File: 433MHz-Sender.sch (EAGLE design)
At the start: 21 parts, among them IC1 LP2950Z, U1 ATTINY85V-10S

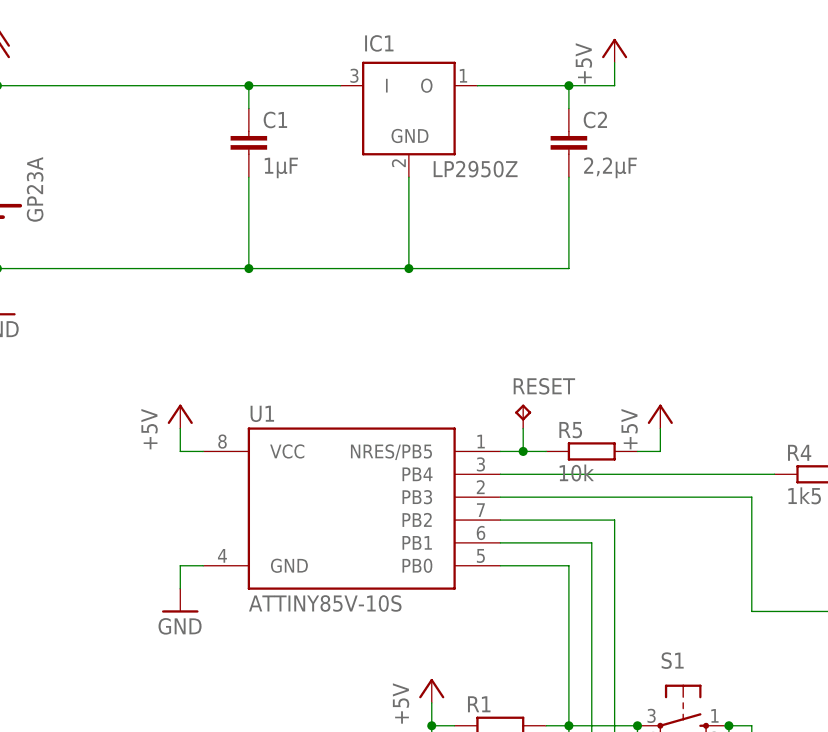
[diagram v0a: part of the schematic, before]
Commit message: 433MHz-Server und IO-Board-2 Anpassungen
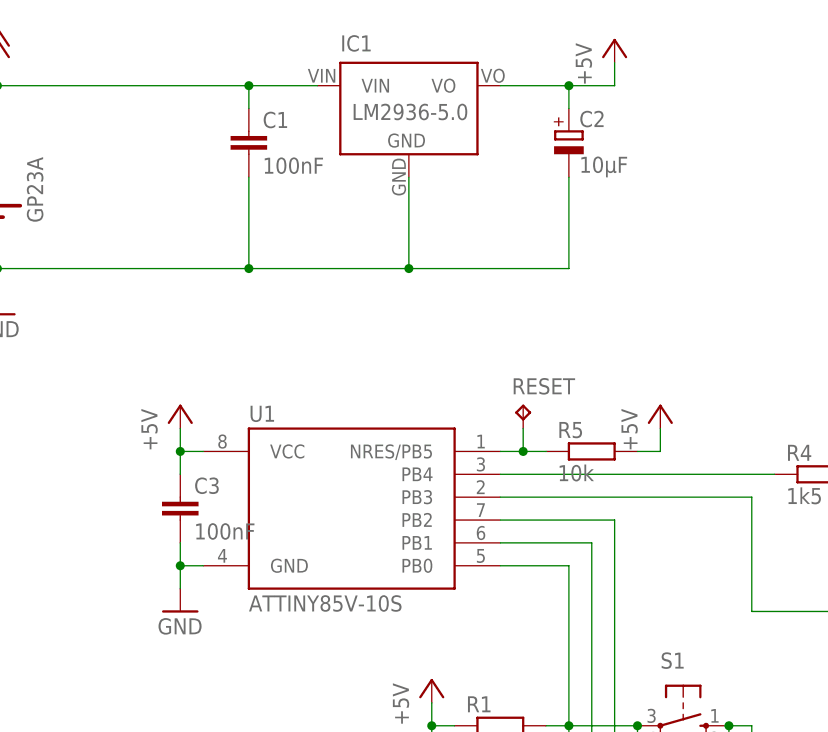
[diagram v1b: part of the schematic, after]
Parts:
- added C3: 100nF, rcl:C-EU025-025X050
- C1: value 1µF -> 100nF
- C2: value 2,2µF -> 10µF; device rcl:C-EU025-025X050 -> rcl:CPOL-EUE2-4
- IC1: value LP2950Z -> LM2936-5.0; device linear:LP2950Z -> LM2936:LM2936-5.0
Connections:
- net +12V: now also IC1.VIN; no longer IC1.I
- net +5V: now also C2.+, C3.1, IC1.VO; no longer C2.1, IC1.O
- net GND: now also C2.-, C3.2; no longer C2.2
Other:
- moved on the sheet: IC1
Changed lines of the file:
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@@
 <setting verticaltext="up"/>
 </settings>
-<grid distance="0.1" unitdist="inch" unit="inch" style="dots" multiple="1" display="yes" altdistance="0.01" altunitdist="inch" altunit="inch"/>
+<grid distance="0.1" unitdist="inch" unit="inch" style="lines" multiple="1" display="no" altdistance="0.01" altunitdist="inch" altunit="inch"/>
 <layers>
 <layer number="1" name="Top" color="4" fill="1" visible="no" active="no"/>
@@
 <part name="P+1" library="supply1" deviceset="+12V" device=""/>
 <part name="GND1" library="supply1" deviceset="GND" device=""/>
-<part name="IC1" library="linear" deviceset="LP2950" device="Z"/>
-<part name="C1" library="rcl" deviceset="C-EU" device="025-025X050" value="1µF"/>
-<part name="C2" library="rcl" deviceset="C-EU" device="025-025X050" value="2,2µF"/>
+<part name="C1" library="rcl" deviceset="C-EU" device="025-025X050" value="100nF"/>
 <part name="P+2" library="supply1" deviceset="+5V" device=""/>
 <part name="P+3" library="supply1" deviceset="+5V" device=""/>
@@
 <part name="R5" library="rcl" deviceset="R-EU_" device="0204/5" value="10k"/>
 <part name="P+6" library="supply1" deviceset="+5V" device=""/>
+<part name="C3" library="rcl" deviceset="C-EU" device="025-025X050" value="100nF"/>
+<part name="IC1" library="LM2936" deviceset="LM2936?*" device="" technology="-5.0"/>
+<part name="C2" library="rcl" deviceset="CPOL-EU" device="E2-4" value="10µF"/>
 </parts>
 <sheets>
@@
 <instance part="P+1" gate="1" x="22.86" y="116.84"/>
 <instance part="GND1" gate="1" x="22.86" y="86.36"/>
-<instance part="IC1" gate="G$1" x="68.58" y="109.22"/>
 <instance part="C1" gate="G$1" x="50.8" y="106.68"/>
-<instance part="C2" gate="G$1" x="86.36" y="106.68"/>
 <instance part="P+2" gate="1" x="91.44" y="116.84"/>
 <instance part="P+3" gate="1" x="43.18" y="76.2"/>
@@
 <instance part="R5" gate="G$1" x="88.9" y="71.12"/>
 <instance part="P+6" gate="1" x="96.52" y="76.2"/>
+<instance part="C3" gate="G$1" x="43.18" y="66.04"/>
+<instance part="IC1" gate="G$1" x="68.58" y="109.22"/>
+<instance part="C2" gate="G$1" x="86.36" y="106.68"/>
 </instances>
 <busses>
@@
 <wire x1="50.8" y1="91.44" x2="22.86" y2="91.44" width="0.1524" layer="91"/>
 <junction x="22.86" y="91.44"/>
+<junction x="50.8" y="91.44"/>
+<wire x1="50.8" y1="91.44" x2="68.58" y2="91.44" width="0.1524" layer="91"/>
+<pinref part="C2" gate="G$1" pin="-"/>
+<wire x1="68.58" y1="91.44" x2="86.36" y2="91.44" width="0.1524" layer="91"/>
+<wire x1="86.36" y1="101.6" x2="86.36" y2="91.44" width="0.1524" layer="91"/>
 <pinref part="IC1" gate="G$1" pin="GND"/>
-<wire x1="50.8" y1="91.44" x2="68.58" y2="91.44" width="0.1524" layer="91"/>
-<wire x1="68.58" y1="91.44" x2="68.58" y2="101.6" width="0.1524" layer="91"/>
-<junction x="50.8" y="91.44"/>
-<pinref part="C2" gate="G$1" pin="2"/>
-<wire x1="68.58" y1="91.44" x2="86.36" y2="91.44" width="0.1524" layer="91"/>
-<wire x1="86.36" y1="91.44" x2="86.36" y2="101.6" width="0.1524" layer="91"/>
+<wire x1="68.58" y1="101.6" x2="68.58" y2="91.44" width="0.1524" layer="91"/>
 <junction x="68.58" y="91.44"/>
 </segment>
@@
 <wire x1="45.72" y1="58.42" x2="43.18" y2="58.42" width="0.1524" layer="91"/>
 <wire x1="43.18" y1="58.42" x2="43.18" y2="55.88" width="0.1524" layer="91"/>
+<pinref part="C3" gate="G$1" pin="2"/>
+<wire x1="43.18" y1="60.96" x2="43.18" y2="58.42" width="0.1524" layer="91"/>
+<junction x="43.18" y="58.42"/>
 </segment>
 <segment>
@@
 <wire x1="22.86" y1="111.76" x2="22.86" y2="114.3" width="0.1524" layer="91"/>
 <wire x1="50.8" y1="111.76" x2="50.8" y2="109.22" width="0.1524" layer="91"/>
-<pinref part="IC1" gate="G$1" pin="I"/>
-<wire x1="50.8" y1="111.76" x2="60.96" y2="111.76" width="0.1524" layer="91"/>
 <wire x1="50.8" y1="111.76" x2="22.86" y2="111.76" width="0.1524" layer="91"/>
+<junction x="22.86" y="111.76"/>
+<pinref part="IC1" gate="G$1" pin="VIN"/>
+<wire x1="50.8" y1="111.76" x2="58.42" y2="111.76" width="0.1524" layer="91"/>
 <junction x="50.8" y="111.76"/>
-<junction x="22.86" y="111.76"/>
 </segment>
 <segment>
@@
 <net name="+5V" class="0">
 <segment>
-<pinref part="IC1" gate="G$1" pin="O"/>
-<wire x1="76.2" y1="111.76" x2="86.36" y2="111.76" width="0.1524" layer="91"/>
-<pinref part="C2" gate="G$1" pin="1"/>
-<wire x1="86.36" y1="111.76" x2="86.36" y2="109.22" width="0.1524" layer="91"/>
-<wire x1="86.36" y1="111.76" x2="91.44" y2="111.76" width="0.1524" layer="91"/>
-<junction x="86.36" y="111.76"/>
 <wire x1="91.44" y1="111.76" x2="91.44" y2="114.3" width="0.1524" layer="91"/>
 <pinref part="P+2" gate="1" pin="+5V"/>
+<pinref part="IC1" gate="G$1" pin="VO"/>
+<wire x1="78.74" y1="111.76" x2="86.36" y2="111.76" width="0.1524" layer="91"/>
+<pinref part="C2" gate="G$1" pin="+"/>
+<wire x1="86.36" y1="111.76" x2="91.44" y2="111.76" width="0.1524" layer="91"/>
+<wire x1="86.36" y1="109.22" x2="86.36" y2="111.76" width="0.1524" layer="91"/>
+<junction x="86.36" y="111.76"/>
 </segment>
 <segment>
@@
 <pinref part="U1" gate="G$1" pin="VCC"/>
 <wire x1="43.18" y1="71.12" x2="45.72" y2="71.12" width="0.1524" layer="91"/>
-</segment>
-<segment>
+<pinref part="C3" gate="G$1" pin="1"/>
+<wire x1="43.18" y1="68.58" x2="43.18" y2="71.12" width="0.1524" layer="91"/>
+<junction x="43.18" y="71.12"/>
+</segment>
+<segment>

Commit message: IO-Board-2 Anpassung
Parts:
- R1, R2, R3: value 10k -> 100k
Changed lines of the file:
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@@
 <part name="433_GND" library="testpad" deviceset="TP" device="PAD1-13"/>
 <part name="GND3" library="supply1" deviceset="GND" device=""/>
-<part name="R1" library="rcl" deviceset="R-EU_" device="0204/5" value="10k"/>
-<part name="R2" library="rcl" deviceset="R-EU_" device="0204/5" value="10k"/>
-<part name="R3" library="rcl" deviceset="R-EU_" device="0204/5" value="10k"/>
+<part name="R1" library="rcl" deviceset="R-EU_" device="0204/5" value="100k"/>
+<part name="R2" library="rcl" deviceset="R-EU_" device="0204/5" value="100k"/>
+<part name="R3" library="rcl" deviceset="R-EU_" device="0204/5" value="100k"/>
 <part name="P+4" library="supply1" deviceset="+5V" device=""/>
 <part name="LED1" library="led" deviceset="LED" device="3MM"/>
